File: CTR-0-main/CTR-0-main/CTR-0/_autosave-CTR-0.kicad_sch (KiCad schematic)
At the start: 34 parts, among them J1 USB_C_Receptacle_USB2.0_14P, J2 Conn_01x20, J3 Conn_01x20, J4 Conn_01x03, SW1 SW_Push, U1 RP2040, U2 NCP1117-3.3_SOT223, U3 W25Q128JVS, Y1 12MHz

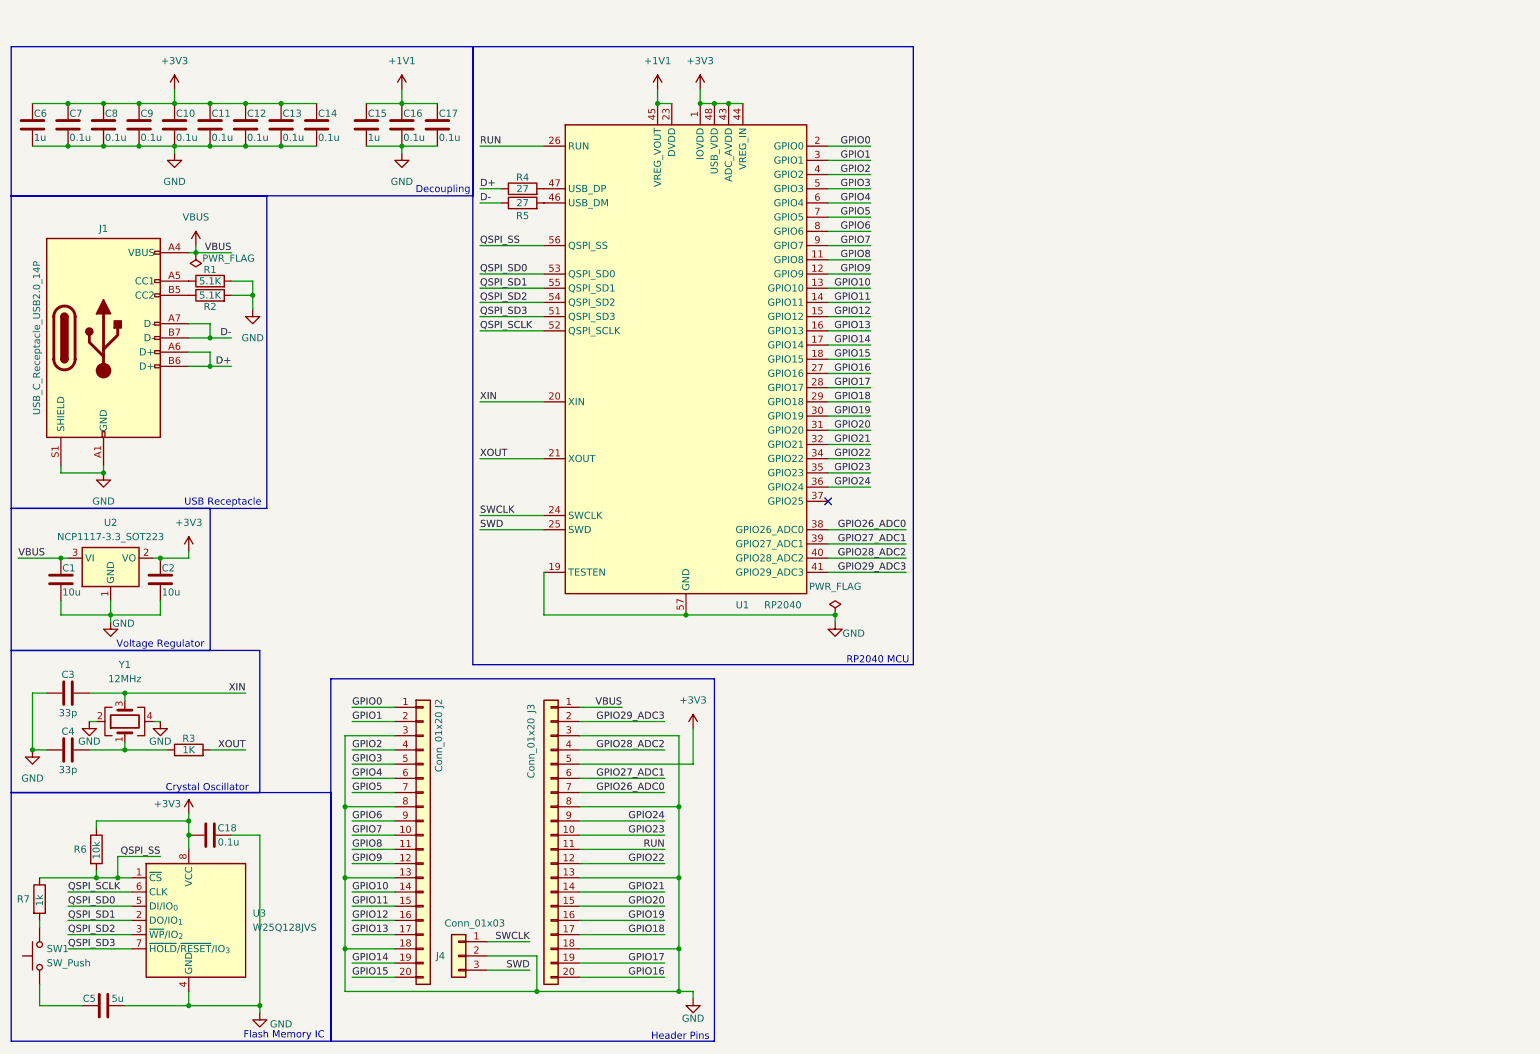
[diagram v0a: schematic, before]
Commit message: reroute #2
does not fulfill drc, fix errors and clearance
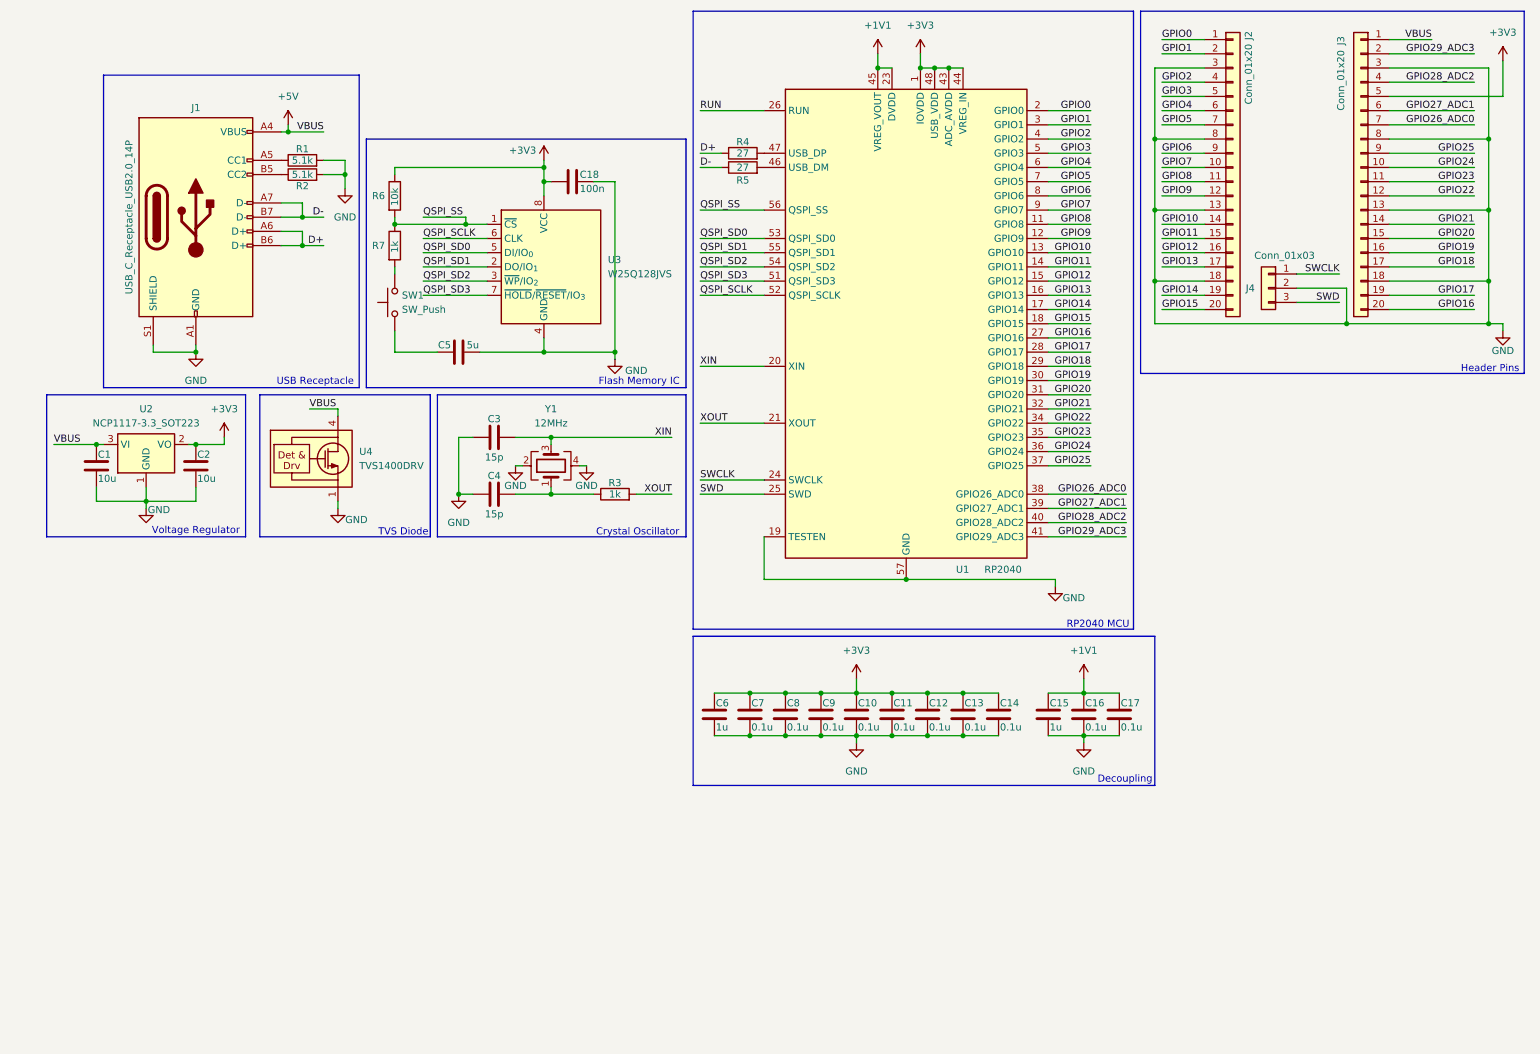
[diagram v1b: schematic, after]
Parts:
- added U4: TVS1400DRV, Package_SON:WSON-6-1EP_2x2mm_P0.65mm_EP1x1.6mm, symbol Power_Protection:TVS1400DRV
- C18: value 0.1u -> 100n
- C3, C4: value 33p -> 15p
- R1, R2: value 5.1K -> 5.1k
- R3: value 1K -> 1k
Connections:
- net GND: now also U4.1 (GND), U4.2 (GND), U4.3 (GND), U4.7 (GND)
- net GPIO23: now also J3.11 (Pin_11); no longer J3.10 (Pin_10)
- net GPIO24: now also J3.10 (Pin_10); no longer J3.9 (Pin_9)
- net RUN: no longer J3.11 (Pin_11)
- net GPIO25: now reaches U1.37 (GPIO25)
- net GPIO25: now also J3.9 (Pin_9)
- net VBUS renamed +5V
- net +5V: now also U4.4 (IN), U4.5 (IN), U4.6 (IN)
- no-connect marks 1 -> 0
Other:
- note added: "TVS Diode"
- moved on the sheet: C1, C10, C11, C12, C13, C14, C15, C16, C17, C18, C2, C3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
